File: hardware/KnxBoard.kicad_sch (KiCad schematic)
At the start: 40 parts

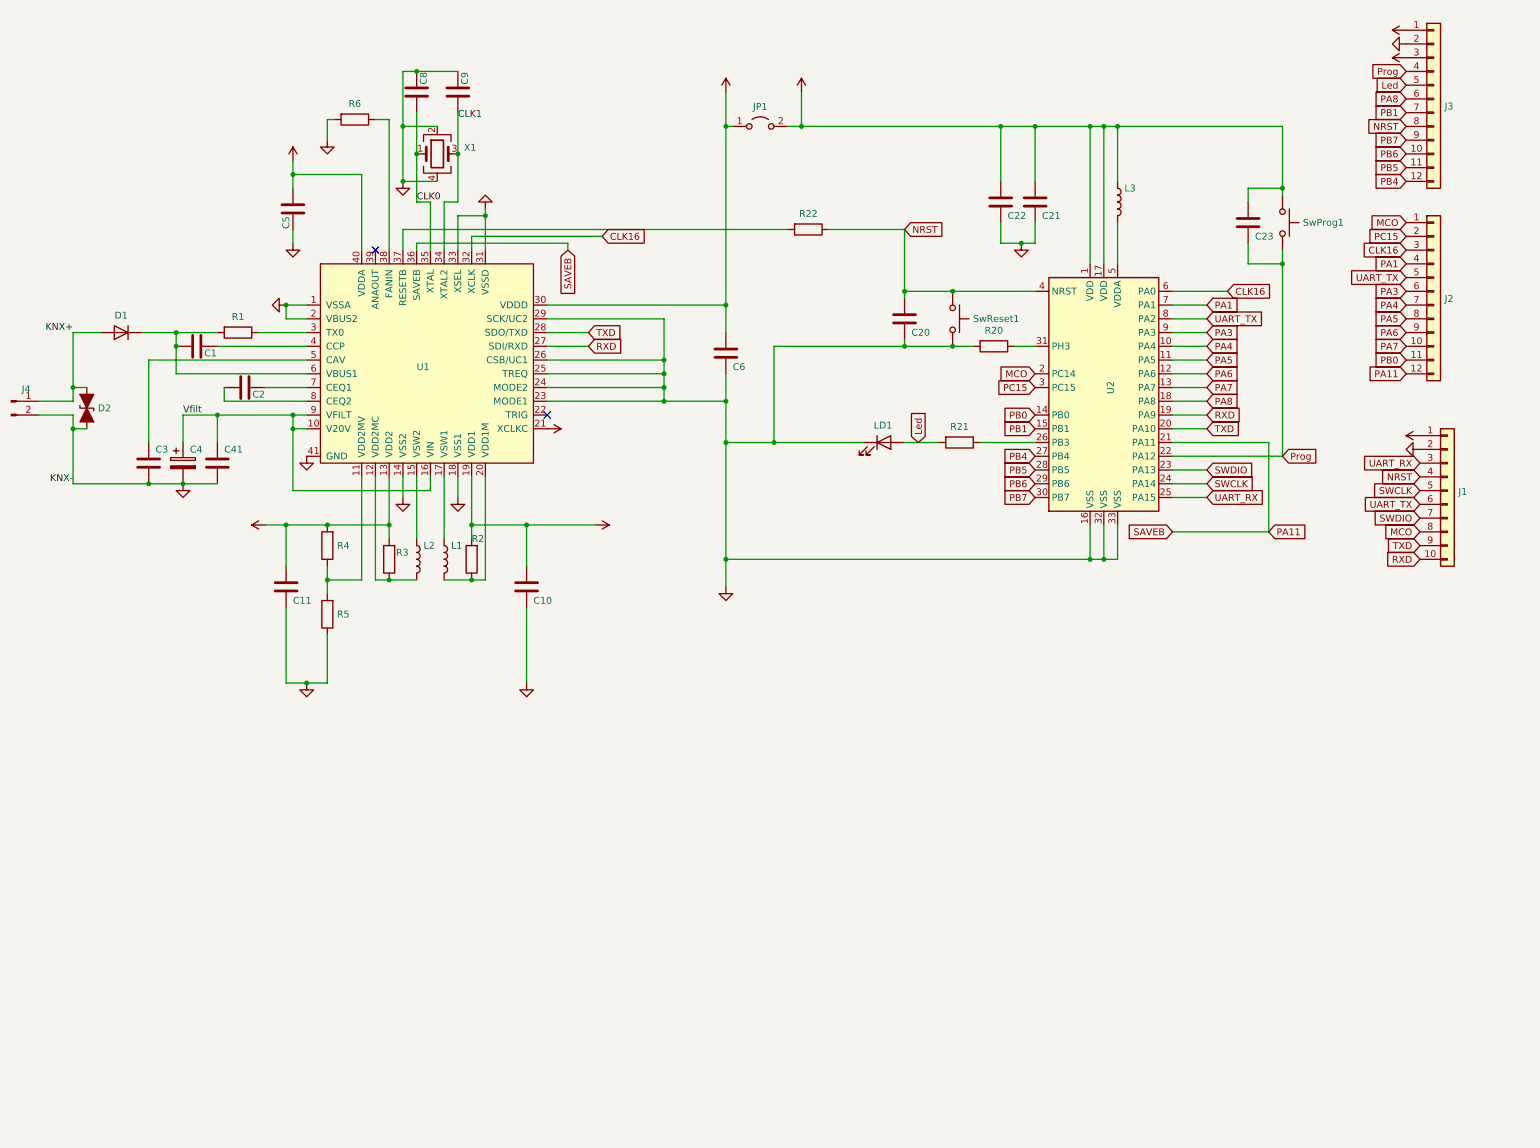
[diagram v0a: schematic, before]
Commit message: Update pcb rules
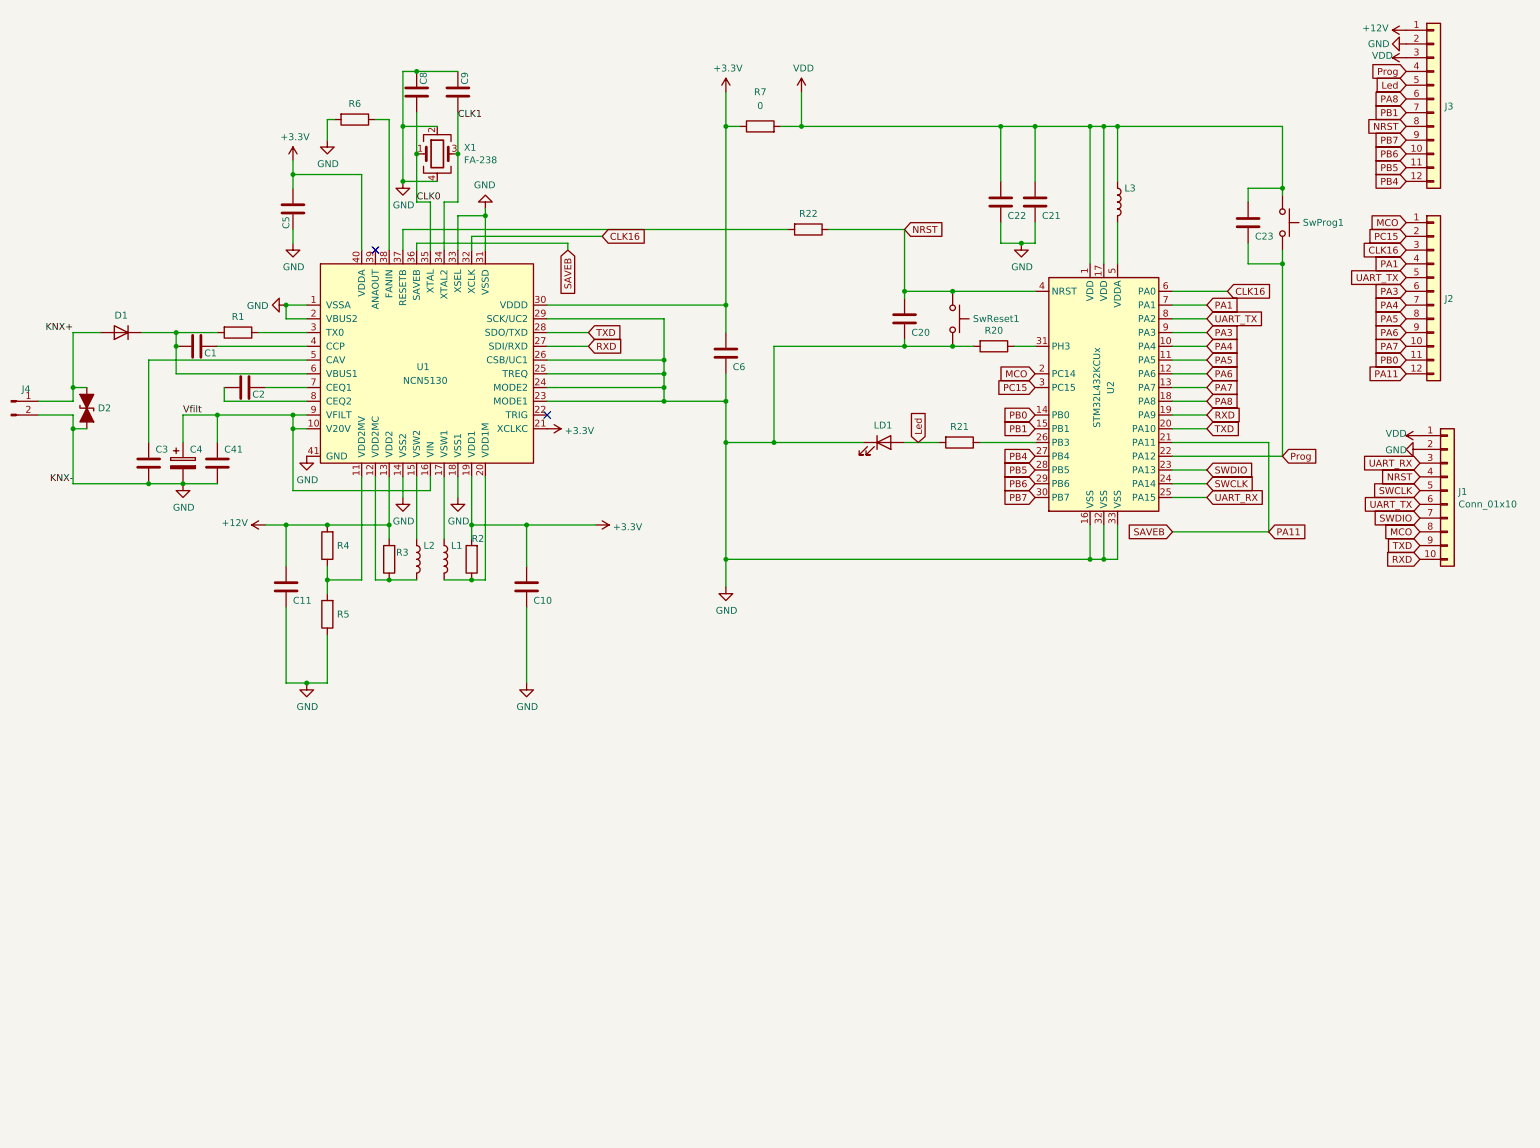
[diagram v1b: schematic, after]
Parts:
- removed JP1: (no value), symbol Jumper:Jumper_2_Open
- added R7: 0, Resistor_SMD:R_0603_1608Metric, symbol Device:R
- C1: value (none) -> 47nF 50V; footprint (none) -> Capacitor_SMD:C_0603_1608Metric
- C10, C11, C22: value (none) -> 10uF 6.3V ESR < 0.1ohm; footprint (none) -> Capacitor_SMD:C_0805_2012Metric
- C2: value (none) -> 220nF 50V; footprint (none) -> Capacitor_SMD:C_0603_1608Metric
- C20, C21, C23, C5, C6: value (none) -> 100nF 6.3V; footprint (none) -> Capacitor_SMD:C_0603_1608Metric
- C3: value (none) -> 100nF 50V; footprint (none) -> Capacitor_SMD:C_0603_1608Metric
- C4: value (none) -> 100uF 35V; footprint (none) -> Capacitor_SMD:CP_Elec_6.3x7.7
- C41: value (none) -> 1uF 35V ESR < 2ohm; footprint (none) -> Capacitor_SMD:C_0603_1608Metric
- C8, C9: value (none) -> 10pF 6.3V; footprint (none) -> Capacitor_SMD:C_0603_1608Metric
- D1: value (none) -> SS16; footprint (none) -> Diode_SMD:D_SMA
- D2: value (none) -> 1SMA40CA; footprint (none) -> Diode_SMD:D_SMA
- J1: value (none) -> Conn_01x10; footprint (none) -> Connector_PinHeader_1.27mm:PinHeader_2x05_P1.27mm_Vertical
- J2, J3: value (none) -> Conn_01x12; footprint (none) -> Connector_PinHeader_2.54mm:PinHeader_1x12_P2.54mm_Vertical
- J4: value (none) -> Conn_01x02_Male; footprint (none) -> KnxBoard:KNX_Connector
- L1, L2, L3: value (none) -> 220uH; footprint (none) -> Inductor_SMD:L_1008_2520Metric
- LD1: value (none) -> LED; footprint (none) -> LED_SMD:LED_0603_1608Metric
- R1: value (none) -> 27R 1W; footprint (none) -> Resistor_SMD:R_0612_1632Metric
- R2, R3: value (none) -> 1R 1/16W; footprint (none) -> Resistor_SMD:R_0603_1608Metric
- R20: value (none) -> 10K 1/16w; footprint (none) -> Resistor_SMD:R_0603_1608Metric
- R21: value (none) -> 100R; footprint (none) -> Resistor_SMD:R_0603_1608Metric
- R22, R6: value (none) -> NOTMOUNT; footprint (none) -> Resistor_SMD:R_0603_1608Metric
- R4: value (none) -> 56K 1/16w; footprint (none) -> Resistor_SMD:R_0603_1608Metric
- R5: value (none) -> 499K 1/16w; footprint (none) -> Resistor_SMD:R_0603_1608Metric
- SwProg1, SwReset1: value (none) -> SW_Push; footprint (none) -> Button_Switch_SMD:SW_SPST_SKQG_WithStem
- U1: value (none) -> NCN5130; footprint (none) -> Package_DFN_QFN:QFN-40-1EP_6x6mm_P0.5mm_EP4.6x4.6mm_ThermalVias
- U2: value (none) -> STM32L432KCUx; footprint (none) -> Package_DFN_QFN:QFN-32-1EP_5x5mm_P0.5mm_EP3.45x3.45mm_ThermalVias
- X1: value (none) -> FA-238; footprint (none) -> Crystal:Crystal_SMD_SeikoEpson_FA238-4Pin_3.2x2.5mm
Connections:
- net +3V3: now also R7.1
- net VDD: now also R7.2

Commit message: Add CAD file for SMT32U575CIU6Q
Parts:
- added U2: STM32U575CIU6Q, KnxBoard:STM32U575CIU6Q, symbol STM32U:STM32U575CIU6Q
- renumbered U2 to U3
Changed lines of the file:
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@@
-    (stroke (width 0) (type default) (color 0 0 0 0))
-  )
-  (wire (pts (xy 214.63 123.19) (xy 147.32 123.19))
     (stroke (width 0) (type default) (color 0 0 0 0))
   )
@@
     (stroke (width 0) (type default) (color 0 0 0 0))
   )
+  (wire (pts (xy 95.25 107.95) (xy 95.25 119.38))
+    (stroke (width 0) (type default) (color 0 0 0 0))
+  )
   (wire (pts (xy 243.84 64.77) (xy 243.84 68.58))
     (stroke (width 0) (type default) (color 0 0 0 0))
@@
     (stroke (width 0) (type default) (color 0 0 0 0))
   )
+  (wire (pts (xy 147.32 123.19) (xy 214.63 123.19))
+    (stroke (width 0) (type default) (color 0 0 0 0))
+  )
   (wire (pts (xy 73.66 146.05) (xy 69.85 146.05))
     (stroke (width 0) (type default) (color 0 0 0 0))
@@
   )
   (wire (pts (xy 97.79 57.15) (xy 97.79 48.26))
-    (stroke (width 0) (type default) (color 0 0 0 0))
-  )
-  (wire (pts (xy 95.25 107.95) (xy 95.25 119.38))
     (stroke (width 0) (type default) (color 0 0 0 0))
   )
@@
   (symbol (lib_id "MCU_ST_STM32L4:STM32L432KCUx") (at 217.17 91.44 0) (unit 1)
     (in_bom yes) (on_board yes)
-    (property "Reference" "U2" (id 0) (at 218.44 91.44 90))
+    (property "Reference" "U3" (id 0) (at 218.44 91.44 90))
     (property "Value" "STM32L432KCUx" (id 1) (at 215.9 91.44 90))
     (property "Footprint" "Package_DFN_QFN:QFN-32-1EP_5x5mm_P0.5mm_EP3.45x3.45mm_ThermalVias" (id 2) (at 207.01 114.3 0)
@@
     (pin "2")
   )
+  (symbol (lib_id "STM32U:STM32U575CIU6Q") (at 156.21 146.05 0) (unit 1)
+    (in_bom yes) (on_board yes) (fields_autoplaced)
+    (property "Reference" "U2" (id 0) (at 186.69 134.62 0)
+      (effects (font (size 1.524 1.524)))
+    )
+    (property "Value" "STM32U575CIU6Q" (id 1) (at 186.69 138.43 0)
+      (effects (font (size 1.524 1.524)))
+    )
+    (property "Footprint" "KnxBoard:STM32U575CIU6Q" (id 2) (at 186.69 139.954 0)
+      (effects (font (size 1.524 1.524)) hide)
+    )
+    (property "Datasheet" "" (id 3) (at 156.21 146.05 0)
+      (effects (font (size 1.524 1.524)))
+    )
+    (pin "1")
+    (pin "10")
+    (pin "11")
+    (pin "12")
+    (pin "13")
+    (pin "14")
+    (pin "15")
+    (pin "16")
+    (pin "17")
+    (pin "18")
+    (pin "19")
+    (pin "2")
+    (pin "20")
+    (pin "21")
+    (pin "22")
+    (pin "23")
+    (pin "24")
+    (pin "25")
+    (pin "26")
+    (pin "27")
+    (pin "28")
+    (pin "29")
+    (pin "3")
+    (pin "30")
+    (pin "31")
+    (pin "32")
+    (pin "33")
+    (pin "34")
+    (pin "35")
+    (pin "36")
+    (pin "37")
+    (pin "38")
+    (pin "39")
+    (pin "4")
+    (pin "40")
+    (pin "41")
+    (pin "42")
+    (pin "43")
+    (pin "44")
+    (pin "45")
+    (pin "46")
+    (pin "47")
+    (pin "48")
+    (pin "49")
+    (pin "5")
+    (pin "6")
+    (pin "7")
+    (pin "8")
+    (pin "9")
+  )
   (sheet_instances
     (path "/" (page "1"))
@@
       (reference "U1") (unit 1) (value "NCN5130") (footprint "Package_DFN_QFN:QFN-40-1EP_6x6mm_P0.5mm_EP4.6x4.6mm_ThermalVias")
     )
+    (path "/e4d7187b-de6c-46e6-95cb-8889cf69b07f"
+      (reference "U2") (unit 1) (value "STM32U575CIU6Q") (footprint "KnxBoard:STM32U575CIU6Q")
+    )
     (path "/00000000-0000-0000-0000-0000618445e2"
-      (reference "U2") (unit 1) (value "STM32L432KCUx") (footprint "Package_DFN_QFN:QFN-32-1EP_5x5mm_P0.5mm_EP3.45x3.45mm_ThermalVias")
+      (reference "U3") (unit 1) (value "STM32L432KCUx") (footprint "Package_DFN_QFN:QFN-32-1EP_5x5mm_P0.5mm_EP3.45x3.45mm_ThermalVias")
     )
     (path "/00000000-0000-0000-0000-0000618e2a33"

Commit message: Create sub-sheet for MCU
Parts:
- removed U2: STM32U575CIU6Q, KnxBoard:STM32U575CIU6Q, symbol STM32U:STM32U575CIU6Q
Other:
- added sheet MCU (mcu.kicad_sch)
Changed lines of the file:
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@@
     (pin "2")
   )
-  (symbol (lib_id "STM32U:STM32U575CIU6Q") (at 156.21 146.05 0) (unit 1)
-    (in_bom yes) (on_board yes) (fields_autoplaced)
-    (property "Reference" "U2" (id 0) (at 186.69 134.62 0)
-      (effects (font (size 1.524 1.524)))
-    )
-    (property "Value" "STM32U575CIU6Q" (id 1) (at 186.69 138.43 0)
-      (effects (font (size 1.524 1.524)))
-    )
-    (property "Footprint" "KnxBoard:STM32U575CIU6Q" (id 2) (at 186.69 139.954 0)
-      (effects (font (size 1.524 1.524)) hide)
-    )
-    (property "Datasheet" "" (id 3) (at 156.21 146.05 0)
-      (effects (font (size 1.524 1.524)))
-    )
-    (pin "1")
-    (pin "10")
-    (pin "11")
-    (pin "12")
-    (pin "13")
-    (pin "14")
-    (pin "15")
-    (pin "16")
-    (pin "17")
-    (pin "18")
-    (pin "19")
-    (pin "2")
-    (pin "20")
-    (pin "21")
-    (pin "22")
-    (pin "23")
-    (pin "24")
-    (pin "25")
-    (pin "26")
-    (pin "27")
-    (pin "28")
-    (pin "29")
-    (pin "3")
-    (pin "30")
-    (pin "31")
-    (pin "32")
-    (pin "33")
-    (pin "34")
-    (pin "35")
-    (pin "36")
-    (pin "37")
-    (pin "38")
-    (pin "39")
-    (pin "4")
-    (pin "40")
-    (pin "41")
-    (pin "42")
-    (pin "43")
-    (pin "44")
-    (pin "45")
-    (pin "46")
-    (pin "47")
-    (pin "48")
-    (pin "49")
-    (pin "5")
-    (pin "6")
-    (pin "7")
-    (pin "8")
-    (pin "9")
+  (sheet (at 231.14 137.16) (size 31.75 19.05) (fields_autoplaced)
+    (stroke (width 0.1524) (type solid) (color 0 0 0 0))
+    (fill (color 0 0 0 0.0000))
+    (property "Sheet name" "MCU" (id 0) (at 231.14 136.4484 0)
+      (effects (font (size 1.27 1.27)) (justify left bottom))
+    )
+    (property "Sheet file" "mcu.kicad_sch" (id 1) (at 231.14 156.7946 0)
+      (effects (font (size 1.27 1.27)) (justify left top))
+    )
   )
   (sheet_instances
     (path "/" (page "1"))
+    (path "/d8441614-dec4-4bc1-b184-c502a3d79ed5" (page "2"))
   )
   (symbol_instances
@@
       (reference "U1") (unit 1) (value "NCN5130") (footprint "Package_DFN_QFN:QFN-40-1EP_6x6mm_P0.5mm_EP4.6x4.6mm_ThermalVias")
     )
-    (path "/e4d7187b-de6c-46e6-95cb-8889cf69b07f"
-      (reference "U2") (unit 1) (value "STM32U575CIU6Q") (footprint "KnxBoard:STM32U575CIU6Q")
-    )
     (path "/00000000-0000-0000-0000-0000618445e2"
       (reference "U3") (unit 1) (value "STM32L432KCUx") (footprint "Package_DFN_QFN:QFN-32-1EP_5x5mm_P0.5mm_EP3.45x3.45mm_ThermalVias")
     )
+    (path "/d8441614-dec4-4bc1-b184-c502a3d79ed5/ea06bc96-3cff-45c0-bbf2-79a6c8f72bbc"
+      (reference "U?") (unit 1) (value "STM32U575CIU6Q") (footprint "KnxBoard:STM32U575CIU6Q")
+    )
     (path "/00000000-0000-0000-0000-0000618e2a33"
